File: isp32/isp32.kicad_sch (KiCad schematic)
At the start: 34 parts

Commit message: ESP32 module
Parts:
- added J?: JTAG-ESP, symbol Connector_Generic:Conn_01x06
- added R? (x3): 10k, symbol Device:R_Small
- added SW?: IO0, symbol Switch:SW_Push
- added SW?: RST, symbol Switch:SW_Push
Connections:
- net +3V3: now also U?.2 (VDD), J?.6 (Pin_6), R?.1, R?.1, R?.1
- net GND: now also U?.1 (GND), U?.15 (GND), U?.38 (GND), U?.39 (GND), J?.1 (Pin_1), SW?.1, SW?.1
- net TMS: now reaches U?.13 (IO14)
- net TMS: now also J?.3 (Pin_3)
- net TDI: now reaches U?.14 (IO12)
- net TDI: now also J?.5 (Pin_5)
- net TCK: now reaches U?.16 (IO13)
- net TCK: now also J?.4 (Pin_4)
- net TDO: now reaches U?.23 (IO15)
- net TDO: now also J?.2 (Pin_2)
- net IO0: now reaches U?.25 (IO0)
- net IO0: now also R?.2, SW?.2
- net IO16: now reaches U?.27 (IO16)
- net IO16: now also R?.2
- net RST: now reaches U?.3 (EN)
- net RST: now also R?.2, SW?.2
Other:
- moved on the sheet: U?

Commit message: Complete sensors and servos
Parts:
- removed C? (x2): 22u, Capacitor_SMD:C_0603_1608Metric, symbol Device:C_Small
- removed C? (x2): 10u, Capacitor_SMD:C_0603_1608Metric, symbol Device:C_Small
- removed D?: LED_Small, LED_SMD:LED_0603_1608Metric, symbol Device:LED_Small
- removed L?: 1u, Inductor_SMD:L_Abracon_ASPI-0630LR, symbol Device:L_Small
- removed POWER?: SW_Push, Button_Switch_SMD:SW_SPST_EVQPE1, symbol Switch:SW_Push
- removed R?: 10k, Resistor_SMD:R_0603_1608Metric, symbol Device:R_Small
- removed R?: 2, Resistor_SMD:R_0603_1608Metric, symbol Device:R_Small
- removed R?: 1k, Resistor_SMD:R_0603_1608Metric, symbol Device:R_Small
- removed R?: 0.5, Resistor_SMD:R_0603_1608Metric, symbol Device:R_Small
- removed U?: IP5306, Package_SO:HTSOP-8-1EP_3.9x4.9mm_P1.27mm_EP2.4x3.2mm, symbol IP5306:IP5306
- added AE?: Antenna, symbol Device:Antenna
- added BZ?: Buzzer, Buzzer_Beeper:Buzzer_Mallory_AST1240MLQ, symbol Device:Buzzer
- added C? (x6): 100n, Capacitor_SMD:C_0603_1608Metric, symbol Device:C_Small
- added C? (x2): 100n, Capacitor_Tantalum_SMD:CP_EIA-3528-12_Kemet-T, symbol Device:C_Small
- added C? (x4): 100n, symbol Device:C_Small
- added C?: 10n, Capacitor_SMD:C_0603_1608Metric, symbol Device:C_Small
- added C? (x2): 10u, symbol Device:C_Small
- added C?: 50p, symbol Device:C_Small
- added C?: 1u, Capacitor_Tantalum_SMD:CP_EIA-3528-12_Kemet-T, symbol Device:C_Small
- added C?: 2.2n, symbol Device:C_Small
- added C?: 10u, Capacitor_SMD:C_0603_1608Metric, symbol Device:C_Small
- added C?: 47u, symbol Device:C_Small
- added C?: 10u, Capacitor_Tantalum_SMD:CP_EIA-3528-12_Kemet-T, symbol Device:C_Small
- added D?: GPS_LED, symbol Device:LED_Small
- added D?: WS2812, LED_SMD:LED_WS2812_PLCC6_5.0x5.0mm_P1.6mm, symbol LED:WS2812
- added J?: GPS_ANT, symbol Connector:Conn_Coaxial
- added J?: I2C_OUT, symbol Connector_Generic_MountingPin:Conn_01x05_MountingPin
- added J?: F0, TerminalBlock_Phoenix:TerminalBlock_Phoenix_MPT-0,5-2-2.54_1x02_P2.54mm_Horizontal, symbol Connector:Screw_Terminal_01x02
- added J?: F1, TerminalBlock_Phoenix:TerminalBlock_Phoenix_MPT-0,5-2-2.54_1x02_P2.54mm_Horizontal, symbol Connector:Screw_Terminal_01x02
- added JP?: PS_USB_D-, symbol Jumper:Jumper_2_Open
- added JP?: PS_USB_D+, symbol Jumper:Jumper_2_Open
- added L?: 22u, symbol Device:L_Small
- added L?: 10u, symbol Device:L_Small
- added M? (x4): Motor_Servo, symbol Motor:Motor_Servo
- added Q? (x3): BSS138, Package_TO_SOT_SMD:SOT-23, symbol Transistor_FET:BSS138
- added Q? (x2): IRLML6402, Package_TO_SOT_SMD:SOT-23, symbol Transistor_FET:IRLML6402
- added Q? (x2): S8050, Package_TO_SOT_SMD:SOT-23, symbol Transistor_BJT:S8050
- added R? (x2): 4k7, symbol Device:R_Small
- added R? (x6): 10k, symbol Device:R_Small
- added R? (x6): 100K, Resistor_SMD:R_0603_1608Metric, symbol Device:R_Small
- added R? (x2): 470, Resistor_SMD:R_0603_1608Metric, symbol Device:R_Small
- added R?: 330, symbol Device:R_Small
- added R? (x2): 10k, Resistor_SMD:R_0603_1608Metric, symbol Device:R_Small
- added R?: 100k, symbol Device:R_Small
- added R?: 91k, symbol Device:R_Small
- added R?: 22, symbol Device:R_Small
- added R?: 52.5k, symbol Device:R_Small
- added SW?: PL_RST, symbol Switch:SW_Push
- added U?: RFM98W-315S2, RF_Module:HOPERF_RFM9XW_SMD, symbol RF_Module:RFM98W-315S2
- added U?: NEO-XM, RF_GPS:ublox_NEO, symbol RF_GPS:NEO-M8M
- added U?: MPU-9250, Sensor_Motion:InvenSense_QFN-24_3x3mm_P0.4mm, symbol Sensor_Motion:MPU-9250
- added U?: BMP280, Package_LGA:Bosch_LGA-8_2x2.5mm_P0.65mm_ClockwisePinNumbering, symbol Sensor_Pressure:BMP280
- added U?: MP2303ADN, Package_SO:SOIC-8-1EP_3.9x4.9mm_P1.27mm_EP2.62x3.51mm, symbol Regulator_Switching:MP2303ADN
- added U?: CH340C, Package_SO:SOIC-16_3.9x9.9mm_P1.27mm, symbol Interface_USB:CH340C
- X?: value ASE-xxxMHz -> ASE-25MHz
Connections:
- net VBUS is gone; now on net +5V: J?.A4 (VBUS), J?.A9 (VBUS), J?.B4 (VBUS), J?.B9 (VBUS), U?.5 (VBUS)
- net +1V2: now also U?.D4 (VCC), U?.D8 (VCC), U?.H4 (VCC), U?.H8 (VCC)
- net +3V3: now also U?.8 (VCC), U?.C10 (VPP_2V5), U?.D6 (VCCIO_0), U?.E4 (VCCIO_3), U?.F8 (VCCIO_1), U?.G4 (VCCIO_3), U?.H6 (VCCIO_2), U?.L11 (VCC_SPI), X?.4 (Vdd), C?.1, C?.1, C?.1, C?.1, C?.1, C?.1, C?.1, C?.1, J?.1 (Pin_1), Q?.1 (G), Q?.1 (G), Q?.1 (G), R?.1, R?.1, R?.1, R?.1, R?.1, R?.1, R?.1, R?.1, R?.1, R?.1, R?.1, U?.1 (RESV_VDDIO), U?.13 (3.3V), U?.13 (VDD), U?.16 (VCC), U?.22 (V_BCKP), U?.23 (VCC), U?.6 (VDDIO), U?.8 (VDD), U?.8 (VDDIO), U?.8 (~{RESET}), U?.9 (VCC_RF)
- net +5V: now also C?.1, D?.3 (VCC), D?.5 (VDD), L?.2, M?.2 (+), M?.2 (+), M?.2 (+), M?.2 (+), R?.1, R?.2
- net +BATT: now also C?.1, C?.1, Q?.2 (S), Q?.2 (S), R?.1, R?.1, R?.1, U?.2 (IN)
- net D+: now also JP?.1 (A)
- net D-: now also JP?.1 (A)
- net GND: now also U?.4 (GND), U?.E5 (GND), U?.E6 (GND), U?.E7 (GND), U?.F5 (GND), U?.F6 (GND), U?.F7 (GND), U?.G5 (GND), U?.G6 (GND), U?.G7 (GND), U?.H5 (GND), X?.2 (GND), BZ?.2 (+), C?.2, C?.2, C?.2, C?.2, C?.2, C?.2, C?.2, C?.2, C?.2, C?.2, C?.2, C?.2, C?.2, C?.2, C?.2, C?.2, D?.1 (K), D?.6 (VSS), J?.2 (Ext), J?.2 (Pin_2), J?.2 (Pin_2), J?.2 (Pin_2), J?.MP (MountPin), M?.3 (-), M?.3 (-), M?.3 (-), M?.3 (-), R?.2, R?.2, SW?.1, U?.1 (GND), U?.1 (GND), U?.1 (GND), U?.10 (GND), U?.10 (GND), U?.11 (FSYNC), U?.12 (GND), U?.13 (GND), U?.18 (GND), U?.2 (D_SEL), U?.20 (RESV_GND), U?.24 (GND), U?.4 (GND), U?.7 (GND), U?.8 (GND)
- net IO0: now also Q?.2 (S), Q?.3 (C), R?.2
- net RST: now also Q?.3 (C)
- net PL_RST: now reaches U?.L9 (~{CRESET})
- net PL_RST: now also R?.2, SW?.2
- net at U?.C5 (GNDPLL1): now also C?.2, C?.2
- net at U?.C6 (VCCPLL1): now also C?.1, C?.1
- net at U?.J6 (VCCPLL0): now also C?.1, C?.1
- net MISO: now reaches U?.J9 (IOB_106_SDI)
- net MISO: now also U?.2 (SO/IO1), U?.31 (IO19), U?.2 (MISO), U?.20 (TXD/SPI_MISO), U?.9 (AD0/MISO)
- net MOSI: now reaches U?.K9 (IOB_105_SDO)
- net MOSI: now also U?.37 (IO23), U?.5 (SI/IO0), U?.21 (RXD/SPI_MOSI), U?.24 (SDA/MOSI), U?.3 (MOSI)
- net SCK: now reaches U?.L10 (IOB_107_SCK)
- net SCK: now also U?.30 (IO18), U?.6 (SCK), U?.19 (SCL/SPI_CLK), U?.23 (SCL/SCLK), U?.4 (SCK)
- net at U?.L6 (GNDPLL0): now also C?.2, C?.2
- net GPS_SS: now reaches U?.10 (IO25)
- net GPS_SS: now also R?.2, U?.18 (SDA/~{SPI_CS})
- net IMU_SS: now reaches U?.11 (IO26)
- net IMU_SS: now also R?.2, U?.22 (~{CS})
- net LORA_SS: now reaches U?.12 (IO27)
- net LORA_SS: now also R?.2, U?.5 (NSS)
- net FLASH_SS: now reaches U?.24 (IO2)
- net FLASH_SS: now also U?.1 (~{CS})
- net SERVO1: now reaches U?.26 (IO4)
- net SERVO1: now also M?.1 (PWM)
- net SERVO3: now reaches U?.28 (IO17)
- net SERVO3: now also M?.1 (PWM)
- net SERVO2: now reaches U?.29 (IO5)
- net SERVO2: now also M?.1 (PWM)
- net SDA: now reaches U?.33 (IO21)
- net SDA: now also R?.2, U?.3 (SDI)
- net TXD: now reaches U?.34 (RXD0/IO3)
- net TXD: now also R?.1
- net RXD: now reaches U?.35 (TXD0/IO1)
- net RXD: now also R?.1
- net SCL: now reaches U?.36 (IO22)
- net SCL: now also J?.4 (Pin_4), J?.5 (Pin_5), R?.2, U?.4 (SCK)
- net FIRE0: now reaches U?.8 (IO32)
- net FIRE0: now also Q?.2 (S), R?.2
- net FIRE1: now reaches U?.9 (IO33)
- net FIRE1: now also Q?.2 (S), R?.2
- net at X?.1 (EN): now also C?.1
- net PL_CLK: now reaches X?.3 (OUT)
- net IO16 renamed SERVO0
- net SERVO0: now also M?.1 (PWM)
- new net: Q?.1 (G), Q?.3 (D), R?.2 (x2)
- new net: AE?.1 (A), U?.9 (ANT)
- new net: C?.1, U?.4 (V3)
- new net: J?.1 (Pin_1), Q?.3 (D) (x2)
- new net: R?.2, U?.3 (RXD)
- new net: J?.1 (In), L?.2, U?.11 (RF_IN)
- new net: R?.1, U?.3 (TIMEPULSE)
- new net: C?.1, U?.10 (REGOUT)
- new net: L?.1, R?.2
- new net: R?.2, U?.2 (CSB)
- new net: D?.2 (A), R?.2
- new net: Q?.1 (E), R?.1, U?.13 (~{DTR})
- new net: Q?.2 (B), R?.2 (x2)
- new net: C?.1, C?.1, U?.6 (COMP)
- new net: C?.1, U?.8 (SS)
- new net: D?.2 (DIN), Q?.3 (D), R?.2
- new net: Q?.1 (E), R?.1, U?.14 (~{RTS})
- new net: R?.2, U?.2 (TXD)
- new net: C?.2, R?.1
- new net: L?.1, U?.1 (BS), U?.3 (SW)
- new net: R?.2, U?.7 (EN)
- new net: R?.1, R?.1, U?.5 (FB)
- new net Buzz: BZ?.1 (-)
- new net EXT_INT: J?.3 (Pin_3)
- new net PS_D+: JP?.2 (B), U?.5 (UD+)
- new net PS_D-: JP?.2 (B), U?.6 (UD-)
- no-connect marks 2 -> 34
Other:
- note added: "Buzzer"
- note added: "GPS"
- note added: "IMU"
- note added: "Ignition"
- note added: "LoRa"
- note added: "Power"
- note added: "Pressure Sensor"
- note added: "Processing System"
- note added: "Programmable Logic"
- note added: "RGB Indicator"
- note added: "Servo Motors"
- note added: "USB To UART"
- moved on the sheet: J?, R?, SW?, U?, U?A, U?B, U?C, U?D, U?E, X?

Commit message: Change GPS to I2C
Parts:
- removed R?: 10k, symbol Device:R_Small
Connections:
- net +3V3: now also U?.2 (D_SEL)
- net Buzz: now also U?.10 (IO25)
- net GND: no longer U?.2 (D_SEL)
- net MISO: no longer U?.20 (TXD/SPI_MISO)
- net MOSI: no longer U?.21 (RXD/SPI_MOSI), U?.24 (SDA/MOSI)
- net SCK: no longer U?.19 (SCL/SPI_CLK), U?.23 (SCL/SCLK)
- net SCL: now also U?.19 (SCL/SPI_CLK), U?.23 (SCL/SCLK)
- net SDA: now also U?.18 (SDA/~{SPI_CS}), U?.24 (SDA/MOSI)
- removed net GPS_SS: U?.10 (IO25), U?.18 (SDA/~{SPI_CS})
- no-connect marks 34 -> 37
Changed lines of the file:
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@@
   (junction (at 167.005 135.89) (diameter 0) (color 0 0 0 0)
   )
+  (junction (at 180.975 166.37) (diameter 0) (color 0 0 0 0)
+  )
   (junction (at 256.54 231.14) (diameter 0) (color 0 0 0 0)
   )
@@
   (junction (at 276.86 290.068) (diameter 0) (color 0 0 0 0)
   )
-  (junction (at 198.755 173.99) (diameter 0) (color 0 0 0 0)
-  )
   (junction (at 240.665 97.79) (diameter 0) (color 0 0 0 0)
   )
@@
   (no_connect (at 434.34 43.815))
   (no_connect (at 253.365 40.64))
+  (no_connect (at -99.06 3.81))
   (no_connect (at 253.365 53.34))
   (no_connect (at 434.34 41.275))
+  (no_connect (at 180.975 143.51))
   (no_connect (at 313.055 153.67))
   (no_connect (at 180.975 138.43))
@@
   (no_connect (at 253.365 90.17))
   (no_connect (at 253.365 50.8))
+  (no_connect (at 180.975 146.05))
   (no_connect (at 253.365 43.18))
   (no_connect (at 180.975 158.75))
@@
     (stroke (width 0) (type default) (color 0 0 0 0))
   )
-  (wire (pts (xy 180.975 173.99) (xy 198.755 173.99))
-    (stroke (width 0) (type default) (color 0 0 0 0))
-  )
   (polyline (pts (xy 471.17 66.675) (xy 370.205 66.675))
     (stroke (width 0) (type default) (color 0 0 0 0))
@@
     (stroke (width 0) (type default) (color 0 0 0 0))
   )
-  (wire (pts (xy 180.975 168.91) (xy 180.975 173.99))
-    (stroke (width 0) (type default) (color 0 0 0 0))
-  )
   (polyline (pts (xy 471.17 20.32) (xy 471.17 66.675))
     (stroke (width 0) (type default) (color 0 0 0 0))
@@
     (stroke (width 0) (type default) (color 0 0 0 0))
   )
+  (wire (pts (xy 180.975 166.37) (xy 180.975 168.91))
+    (stroke (width 0) (type default) (color 0 0 0 0))
+  )
   (wire (pts (xy 287.655 36.83) (xy 287.655 39.37))
     (stroke (width 0) (type default) (color 0 0 0 0))
@@
     )
   )
-  (global_label "SCK" (shape input) (at 348.615 153.67 0) (fields_autoplaced)
+  (global_label "SCL" (shape input) (at 348.615 153.67 0) (fields_autoplaced)
     (effects (font (size 1.27 1.27)) (justify left))
-    (property "Intersheet References" "${INTERSHEET_REFS}" (id 0) (at 354.7776 153.7494 0)
+    (property "Intersheet References" "${INTERSHEET_REFS}" (id 0) (at 354.5357 153.5906 0)
       (effects (font (size 1.27 1.27)) (justify left) hide)
     )
@@
     )
   )
-  (global_label "SCK" (shape input) (at 180.975 153.67 180) (fields_autoplaced)
+  (global_label "SCL" (shape input) (at 180.975 153.67 180) (fields_autoplaced)
     (effects (font (size 1.27 1.27)) (justify right))
-    (property "Intersheet References" "${INTERSHEET_REFS}" (id 0) (at 174.8124 153.5906 0)
+    (property "Intersheet References" "${INTERSHEET_REFS}" (id 0) (at 175.0543 153.5906 0)
       (effects (font (size 1.27 1.27)) (justify right) hide)
     )
@@
     )
   )
-  (global_label "GPS_SS" (shape input) (at 180.975 151.13 180) (fields_autoplaced)
+  (global_label "SDA" (shape input) (at 180.975 151.13 180) (fields_autoplaced)
     (effects (font (size 1.27 1.27)) (justify right))
-    (property "Intersheet References" "${INTERSHEET_REFS}" (id 0) (at 171.4257 151.0506 0)
+    (property "Intersheet References" "${INTERSHEET_REFS}" (id 0) (at 174.9938 151.0506 0)
       (effects (font (size 1.27 1.27)) (justify right) hide)
     )
@@
     )
   )
-  (global_label "MISO" (shape input) (at 180.975 143.51 180) (fields_autoplaced)
-    (effects (font (size 1.27 1.27)) (justify right))
-    (property "Intersheet References" "${INTERSHEET_REFS}" (id 0) (at 173.9657 143.4306 0)
-      (effects (font (size 1.27 1.27)) (justify right) hide)
-    )
-  )
   (global_label "FIRE0" (shape input) (at 116.205 174.625 0) (fields_autoplaced)
     (effects (font (size 1.27 1.27)) (justify left))
@@
     )
   )
-  (global_label "MOSI" (shape input) (at 348.615 148.59 0) (fields_autoplaced)
+  (global_label "SDA" (shape input) (at 348.615 148.59 0) (fields_autoplaced)
     (effects (font (size 1.27 1.27)) (justify left))
-    (property "Intersheet References" "${INTERSHEET_REFS}" (id 0) (at 355.6243 148.6694 0)
+    (property "Intersheet References" "${INTERSHEET_REFS}" (id 0) (at 354.5962 148.5106 0)
       (effects (font (size 1.27 1.27)) (justify left) hide)
     )
@@
     )
   )
+  (global_label "Buzz" (shape input) (at 116.205 167.005 0) (fields_autoplaced)
+    (effects (font (size 1.27 1.27)) (justify left))
+    (property "Intersheet References" "${INTERSHEET_REFS}" (id 0) (at 123.0933 167.0844 0)
+      (effects (font (size 1.27 1.27)) (justify left) hide)
+    )
+  )
   (global_label "LORA_SS" (shape input) (at 262.89 54.61 270) (fields_autoplaced)
     (effects (font (size 1.27 1.27)) (justify right))
@@
     )
   )
-  (global_label "GPS_SS" (shape input) (at 158.75 158.75 270) (fields_autoplaced)
-    (effects (font (size 1.27 1.27)) (justify right))
-    (property "Intersheet References" "${INTERSHEET_REFS}" (id 0) (at 158.6706 168.2993 90)
-      (effects (font (size 1.27 1.27)) (justify right) hide)
-    )
-  )
   (global_label "TDO" (shape input) (at 61.595 181.61 0) (fields_autoplaced)
     (effects (font (size 1.27 1.27)) (justify left))
@@
     )
   )
-  (global_label "GPS_SS" (shape input) (at 116.205 167.005 0) (fields_autoplaced)
-    (effects (font (size 1.27 1.27)) (justify left))
-    (property "Intersheet References" "${INTERSHEET_REFS}" (id 0) (at 125.7543 167.0844 0)
-      (effects (font (size 1.27 1.27)) (justify left) hide)
-    )
-  )
   (global_label "SCK" (shape input) (at 116.205 154.305 0) (fields_autoplaced)
     (effects (font (size 1.27 1.27)) (justify left))
@@
     )
   )
-  (global_label "MOSI" (shape input) (at 180.975 146.05 180) (fields_autoplaced)
-    (effects (font (size 1.27 1.27)) (justify right))
-    (property "Intersheet References" "${INTERSHEET_REFS}" (id 0) (at 173.9657 145.9706 0)
-      (effects (font (size 1.27 1.27)) (justify right) hide)
-    )
-  )
   (global_label "PL_RST" (shape input) (at 295.91 220.345 0) (fields_autoplaced)
     (effects (font (size 1.27 1.27)) (justify left))
@@
     )
   )
-  (symbol (lib_id "power:+3V3") (at 158.75 153.67 0) (unit 1)
-    (in_bom yes) (on_board yes) (fields_autoplaced)
-    (property "Reference" "#PWR?" (id 0) (at 158.75 157.48 0)
-      (effects (font (size 1.27 1.27)) hide)
-    )
-    (property "Value" "+3V3" (id 1) (at 158.75 147.955 0))
-    (property "Footprint" "" (id 2) (at 158.75 153.67 0)
-      (effects (font (size 1.27 1.27)) hide)
-    )
-    (property "Datasheet" "" (id 3) (at 158.75 153.67 0)
-      (effects (font (size 1.27 1.27)) hide)
-    )
-    (pin "1")
-  )
   (symbol (lib_id "Transistor_FET:BSS138") (at 337.82 43.815 270) (unit 1)
     (in_bom yes) (on_board yes)
@@
     (pin "1")
   )
-  (symbol (lib_id "Device:R_Small") (at 158.75 156.21 0) (unit 1)
-    (in_bom yes) (on_board yes) (fields_autoplaced)
-    (property "Reference" "R?" (id 0) (at 160.655 154.9399 0)
-      (effects (font (size 1.27 1.27)) (justify left))
-    )
-    (property "Value" "10k" (id 1) (at 160.655 157.4799 0)
-      (effects (font (size 1.27 1.27)) (justify left))
-    )
-    (property "Footprint" "" (id 2) (at 158.75 156.21 0)
-      (effects (font (size 1.27 1.27)) hide)
-    )
-    (property "Datasheet" "~" (id 3) (at 158.75 156.21 0)
-      (effects (font (size 1.27 1.27)) hide)
-    )
-    (pin "1")
-    (pin "2")
-  )
   (symbol (lib_id "Device:C_Small") (at 131.445 86.36 0) (unit 1)
     (in_bom yes) (on_board yes) (fields_autoplaced)
@@
   )
   (symbol_instances
-    (path "/0023bb6d-1adb-4493-bd0d-fe7d5193998c"
-      (reference "#PWR?") (unit 1) (value "+3V3") (footprint "")
-    )
     (path "/01f6df4e-cf4a-40a5-a9c9-c1c916f82940"
       (reference "#PWR?") (unit 1) (value "GND") (footprint "")
@@
       (reference "R?") (unit 1) (value "100K") (footprint "Resistor_SMD:R_0603_1608Metric")
     )
-    (path "/8c7461e4-c794-4064-95e3-b0cc0dffbb16"
-      (reference "R?") (unit 1) (value "10k") (footprint "")
-    )
     (path "/97a22990-ef9e-4aa3-b8a9-3a687af61632"

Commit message: Complete isp32 v1 schemtics
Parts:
- removed C? (x3): 100n, symbol Device:C_Small
- removed C? (x2): 10u, symbol Device:C_Small
- removed C? (x2): 22u, Capacitor_SMD:C_0603_1608Metric, symbol Device:C_Small
- removed JP?: PS_USB_D-, symbol Jumper:Jumper_2_Open
- removed JP?: PS_USB_D+, symbol Jumper:Jumper_2_Open
- removed R?: 10k, symbol Device:R_Small
- removed SW?: PL_RST, symbol Switch:SW_Push
- removed U? (x5): ICE40HX8K-BG121, Package_BGA:BGA-121_9.0x9.0mm_Layout11x11_P0.8mm_Ball0.4mm_Pad0.35mm_NSMD, symbol FPGA_Lattice:ICE40HX8K-BG121
- removed X?: ASE-25MHz, Oscillator:Oscillator_SMD_Abracon_ASE-4Pin_3.2x2.5mm, symbol Oscillator:ASE-xxxMHz
- added C20: 100n, Capacitor_Tantalum_SMD:CP_EIA-3528-12_Kemet-T, symbol Device:C_Small
- added D2: F0_LED, symbol Device:LED_Small
- added D4: F1_LED, symbol Device:LED_Small
- added J8: Flash_SPI, symbol Connector_Generic:Conn_01x06
- added Q6: S8050, Package_TO_SOT_SMD:SOT-23, symbol Transistor_BJT:S8050
- added R22, R25: 1k, symbol Device:R_Small
- added R30, R33: 10k, symbol Device:R_Small
- C1: renamed from C?; value 22u -> 100n
- C10, C7, C8: renamed from C?; footprint (none) -> Capacitor_SMD:C_0201_0603Metric
- J2: renamed from J?; value I2C_OUT -> Switching
- J4: renamed from J?; value JTAG-ESP -> ESP_JTAG
- gave numbers to parts that had none: 78
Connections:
- net PS_D+ is gone; now on net D+: U12.5 (UD+)
- net PS_D- is gone; now on net D-: U12.6 (UD-)
- net +3V3: now also C20.1, J8.6 (Pin_6), R30.1
- net +5V: now also BZ1.1 (-)
- net Buzz: now also Q6.2 (B), R33.1; no longer BZ1.1 (-)
- net FLASH_SS: now also J8.5 (Pin_5), R30.2
- net GND: now also C20.2, D2.1 (K), D4.1 (K), J8.1 (Pin_1), Q6.1 (E), R33.2; no longer BZ1.2 (+)
- net MISO: now also J8.3 (Pin_3)
- net MOSI: now also U11.24 (SDA/MOSI), J8.2 (Pin_2)
- net SCK: now also U11.23 (SCL/SCLK), J8.4 (Pin_4)
- net SCL: no longer U11.23 (SCL/SCLK)
- net SDA: no longer U11.24 (SDA/MOSI)
- net at J6.1 (Pin_1), Q3.3 (D): now also R22.2
- net at J7.1 (Pin_1), Q5.3 (D): now also R25.2
- new net: D2.2 (A), R22.1
- new net: D4.2 (A), R25.1
- new net: BZ1.2 (+), Q6.3 (C)
- no-connect marks 37 -> 39
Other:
- note added: "Debug Port"
- note added: "Flash"
- note removed: "Programmable Logic"
- moved on the sheet: BZ1, C1, C2, C25, C26, C4, C6, C7, J4, J6, J7, Q1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

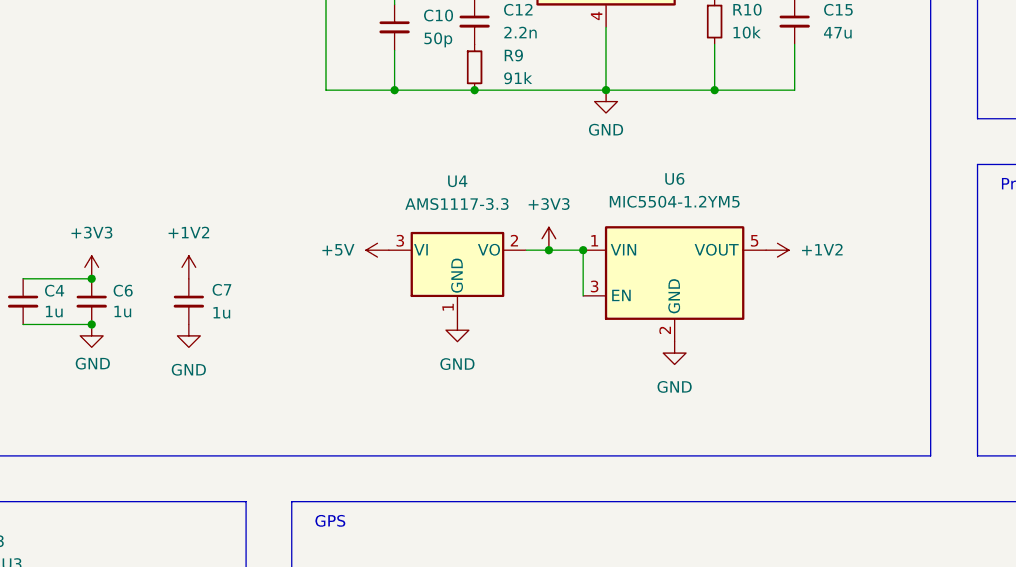
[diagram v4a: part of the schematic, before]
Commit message: Remove 1.2V LDO
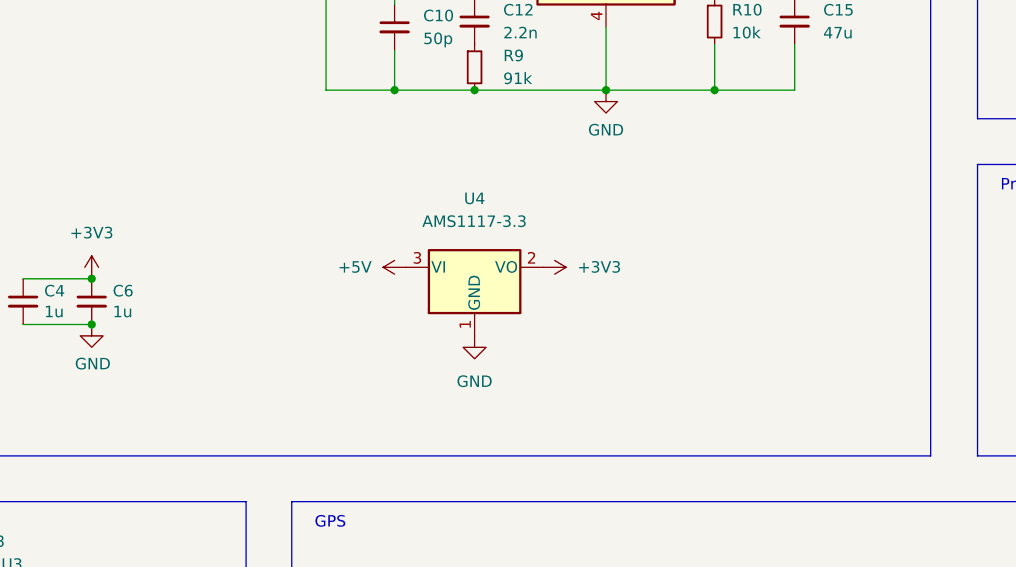
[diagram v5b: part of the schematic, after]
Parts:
- removed C7: 1u, Capacitor_SMD:C_0201_0603Metric, symbol Device:C_Small
- removed U6: MIC5504-1.2YM5, Package_TO_SOT_SMD:SOT-23-5, symbol Regulator_Linear:MIC5504-1.2YM5
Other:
- moved on the sheet: U4

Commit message: Select isp32 footprint
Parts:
- BZ1: footprint Buzzer_Beeper:Buzzer_Mallory_AST1240MLQ -> (none)
- C10, C8: footprint Capacitor_SMD:C_0201_0603Metric -> Capacitor_SMD:C_0603_1608Metric
- C12, C15: footprint (none) -> Capacitor_SMD:C_0603_1608Metric
- C14, C16, C20, C23, C5, C6: footprint Capacitor_Tantalum_SMD:CP_EIA-3528-12_Kemet-T -> Capacitor_SMD:C_0603_1608Metric
- D1, D2, D4: footprint (none) -> LED_SMD:LED_0201_0603Metric
- J2: footprint (none) -> Connector_Molex:Molex_PicoBlade_53261-0571_1x05-1MP_P1.25mm_Horizontal
- J4, J8: footprint (none) -> Connector_PinHeader_1.27mm:PinHeader_1x06_P1.27mm_Vertical
- J5: footprint (none) -> Connector_Coaxial:U.FL_Hirose_U.FL-R-SMT-1_Vertical
- L1, L2: footprint (none) -> Inductor_SMD:L_0201_0603Metric
- M1, M2, M3, M4: footprint (none) -> Connector_PinHeader_2.54mm:PinHeader_1x03_P2.54mm_Vertical
- R1, R10, R11, R12, R13, R14, R15, R17, R2, R22, R25, R3, R30, R33, R4, R6, R8, R9: footprint (none) -> Resistor_SMD:R_0603_1608Metric
- SW1: footprint (none) -> Button_Switch_SMD:SW_SPST_FSMSM
- SW2: footprint (none) -> Button_Switch_SMD:SW_SPST_B3U-1000P

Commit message: Change footprint and layout
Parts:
- removed C3: 10u, Capacitor_SMD:C_0603_1608Metric, symbol Device:C_Small
- removed M1, M2, M3, M4: Motor_Servo, Connector_PinHeader_2.54mm:PinHeader_1x03_P2.54mm_Vertical, symbol Motor:Motor_Servo
- added D5: POWER, LED_SMD:LED_0603_1608Metric, symbol Device:LED_Small
- added J9: Conn_01x12, Connector_PinHeader_2.54mm:PinHeader_1x12_P2.54mm_Horizontal, symbol Connector_Generic:Conn_01x12
- added R18: 1k, Resistor_SMD:R_0603_1608Metric, symbol Device:R_Small
- AE1: footprint (none) -> Connector_PinHeader_2.00mm:PinHeader_1x01_P2.00mm_Vertical
- BZ1: footprint (none) -> Buzzer_Beeper:Buzzer_CUI_CPT-9019S-SMT
- C5: footprint Capacitor_SMD:C_0603_1608Metric -> Capacitor_SMD:C_0805_2012Metric
- D1, D2, D4: footprint LED_SMD:LED_0201_0603Metric -> LED_SMD:LED_0603_1608Metric
- J1: footprint Connector_JST:JST_XH_B2B-XH-A_1x02_P2.50mm_Vertical -> Connector_AMASS:AMASS_XT60-M_1x02_P7.20mm_Vertical
- L1: footprint Inductor_SMD:L_0201_0603Metric -> Inductor_SMD:L_Abracon_ASPI-0630LR
- L2: footprint Inductor_SMD:L_0201_0603Metric -> Inductor_SMD:L_0805_2012Metric
- R22, R25: value 1k -> 10k
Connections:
- net +3V3: now also R18.1
- net +5V: now also J9.11 (Pin_11), J9.2 (Pin_2), J9.5 (Pin_5), J9.8 (Pin_8)
- net GND: now also D5.1 (K), J9.1 (Pin_1), J9.10 (Pin_10), J9.4 (Pin_4), J9.7 (Pin_7)
- net SCL: no longer J2.5 (Pin_5)
- net SDA: now also J2.5 (Pin_5)
- net SERVO0: now also J9.12 (Pin_12)
- net SERVO1: now also J9.6 (Pin_6)
- net SERVO2: now also J9.9 (Pin_9)
- net SERVO3: now also J9.3 (Pin_3)
- new net: D5.2 (A), R18.2
